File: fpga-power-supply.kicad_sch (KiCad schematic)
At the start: 30 parts, among them U14 XC7A100T-FGG484

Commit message: [#55652] Fix hotareas
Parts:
- C145, C151: Manufacturer Samsung -> Samsung Electro-Mechanics
- C150: value C_330u_KEMET_D -> C_Pol_330u_6.3V_KEMET-T520-D; footprint antmicro-footprints:KEMET_D -> antmicro-footprints:C_Pol_EIA-D; symbol antmicroCapacitorspol:C_330u_KEMET_D -> antmicroCapacitorspol:C_Pol_330u_6.3V_KEMET-T520-D; Voltage (none) -> 6.3V
- U14: footprint antmicro-footprints:BGA-484_23x23mm_Layout22x22_P1mm_Xilinx_FGG484 -> antmicro-footprints:BGA-484_23x23mm_Layout22x22_P1mm_FGG484; symbol antmicroMicrocontrollers:XC7A100T-FGG484 -> antmicroFPGAChips:XC7A100T-FGG484; Manufacturer Xilinx -> AMD-Xilinx

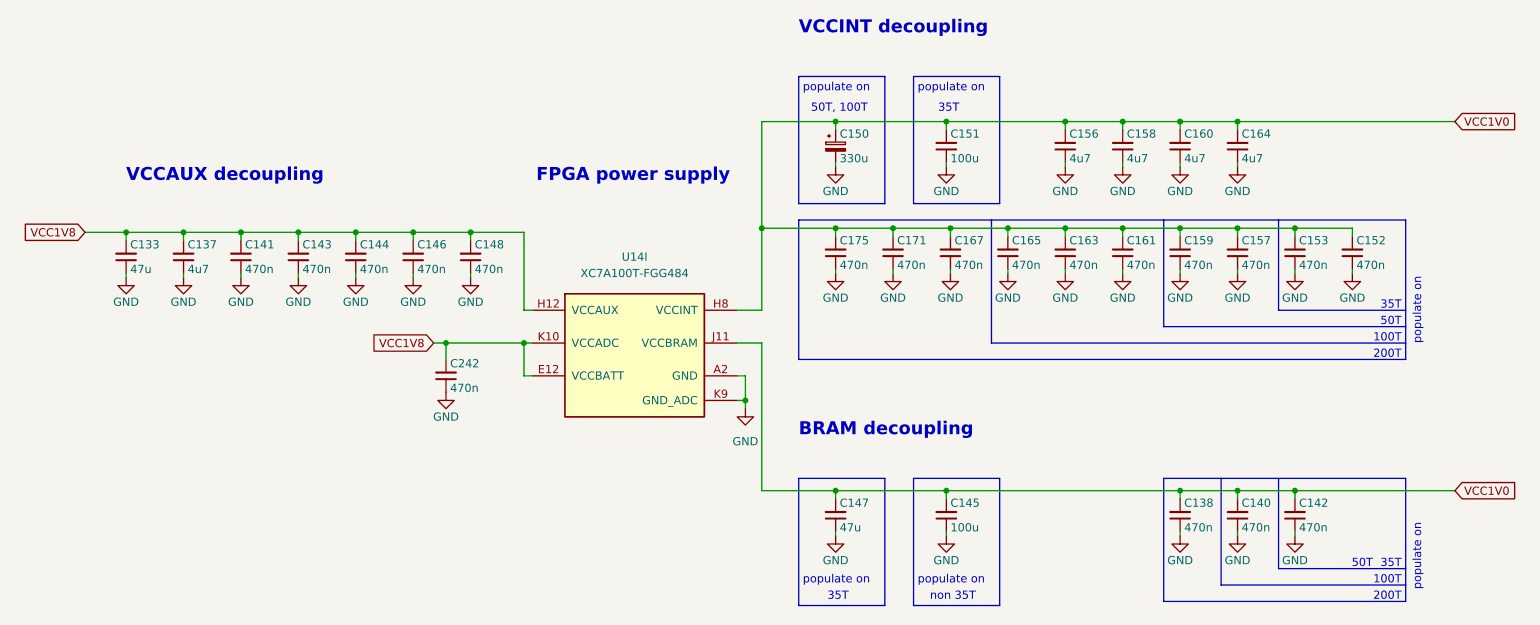
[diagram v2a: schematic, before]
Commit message: [#68236] Allign sch to grid
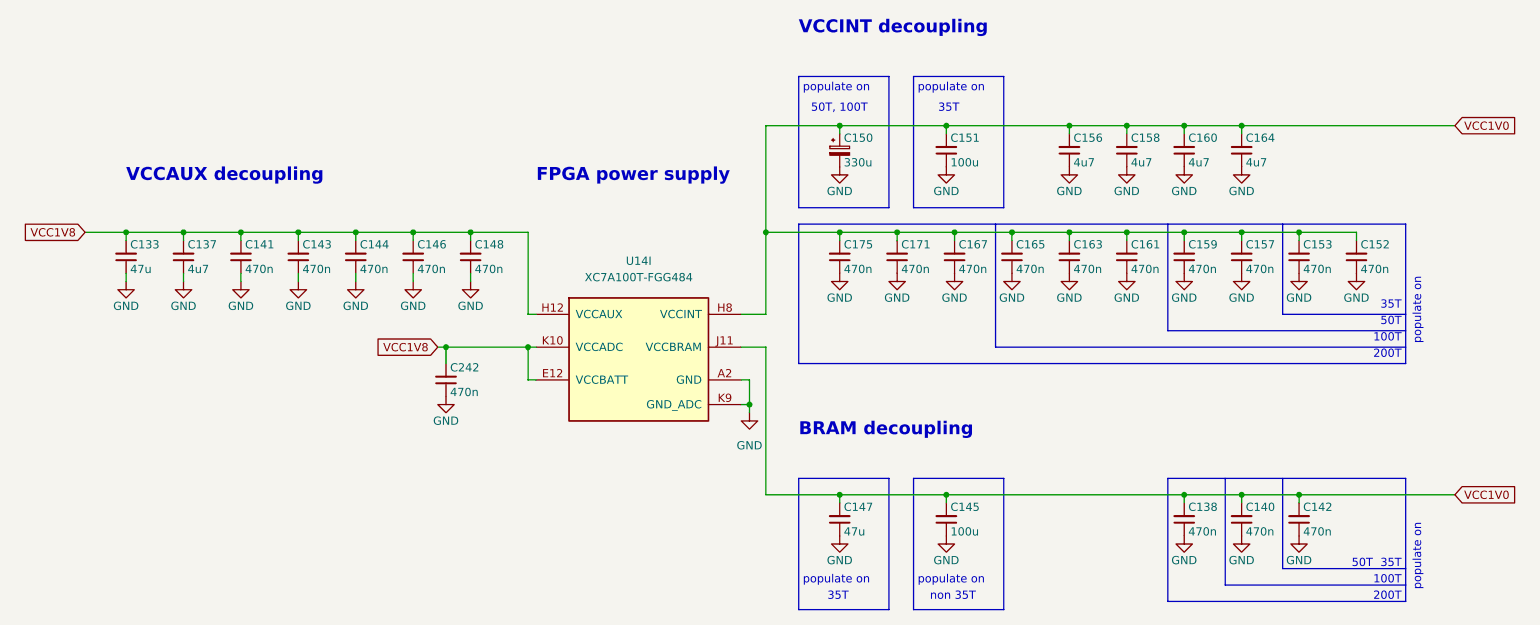
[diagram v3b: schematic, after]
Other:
- moved on the sheet: C138, C140, C142, C145, C147, C150, C151, C152, C153, C156, C157, C158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

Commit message: [#68236] Remove DNP property from Testpoints
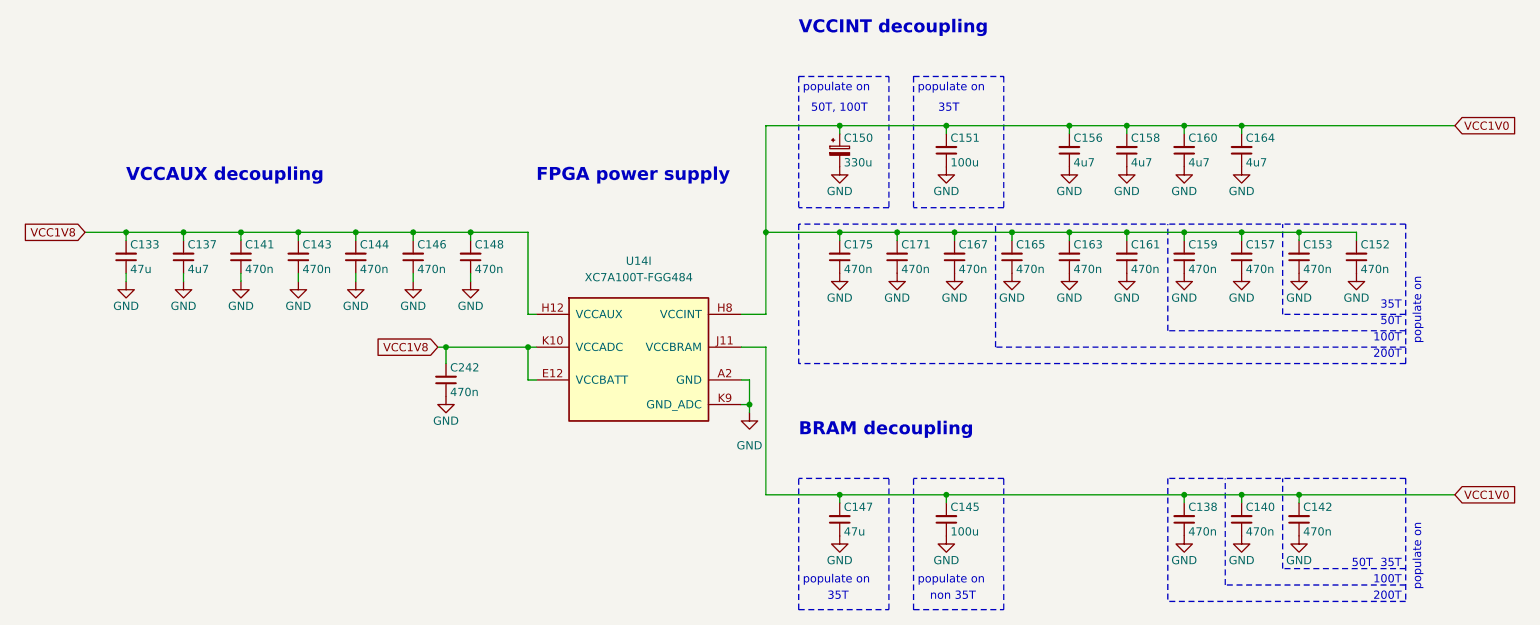
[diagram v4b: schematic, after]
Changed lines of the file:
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@@
   )
   (polyline (pts (xy 242.57 142.24) (xy 242.57 123.19))
-    (stroke (width 0) (type default))
+    (stroke (width 0) (type dash))
   )
   (polyline (pts (xy 306.07 179.07) (xy 278.13 179.07))
-    (stroke (width 0) (type default))
+    (stroke (width 0) (type dash))
   )
   (wire (pts (xy 161.29 124.46) (xy 161.29 125.73))
@@
   )
   (polyline (pts (xy 226.06 100.33) (xy 226.06 120.65))
-    (stroke (width 0) (type default))
+    (stroke (width 0) (type dash))
   )
   (wire (pts (xy 254 107.95) (xy 262.89 107.95))
@@
   )
   (polyline (pts (xy 287.02 137.16) (xy 287.02 123.19))
-    (stroke (width 0) (type default))
+    (stroke (width 0) (type dash))
   )
   (polyline (pts (xy 306.07 144.78) (xy 212.09 144.78))
-    (stroke (width 0) (type default))
+    (stroke (width 0) (type dash))
   )
   (polyline (pts (xy 306.07 142.24) (xy 242.57 142.24))
-    (stroke (width 0) (type default))
+    (stroke (width 0) (type dash))
   )
   (polyline (pts (xy 243.84 162.56) (xy 229.87 162.56))
-    (stroke (width 0) (type default))
+    (stroke (width 0) (type dash))
   )
   (polyline (pts (xy 306.07 144.78) (xy 306.07 123.19))
-    (stroke (width 0) (type default))
+    (stroke (width 0) (type dash))
   )
   (wire (pts (xy 156.21 142.24) (xy 157.48 142.24))
@@
   )
   (polyline (pts (xy 229.87 100.33) (xy 243.84 100.33))
-    (stroke (width 0) (type default))
+    (stroke (width 0) (type dash))
   )
   (wire (pts (xy 236.22 124.46) (xy 227.33 124.46))
@@
   )
   (polyline (pts (xy 287.02 176.53) (xy 287.02 162.56))
-    (stroke (width 0) (type default))
+    (stroke (width 0) (type dash))
   )
   (polyline (pts (xy 229.87 182.88) (xy 229.87 162.56))
-    (stroke (width 0) (type default))
+    (stroke (width 0) (type dash))
   )
   (wire (pts (xy 203.2 147.32) (xy 204.47 147.32))
@@
   )
   (polyline (pts (xy 306.07 162.56) (xy 306.07 181.61))
-    (stroke (width 0) (type default))
+    (stroke (width 0) (type dash))
   )
   (wire (pts (xy 280.67 124.46) (xy 271.78 124.46))
@@
   )
   (polyline (pts (xy 306.07 123.19) (xy 212.09 123.19))
-    (stroke (width 0) (type default))
+    (stroke (width 0) (type dash))
   )
   (polyline (pts (xy 226.06 120.65) (xy 212.09 120.65))
-    (stroke (width 0) (type default))
+    (stroke (width 0) (type dash))
   )
   (wire (pts (xy 203.2 137.16) (xy 207.01 137.16))
@@
   )
   (polyline (pts (xy 212.09 123.19) (xy 212.09 144.78))
-    (stroke (width 0) (type default))
+    (stroke (width 0) (type dash))
   )
   (wire (pts (xy 280.67 124.46) (xy 280.67 125.73))
@@
   )
   (polyline (pts (xy 212.09 182.88) (xy 226.06 182.88))
-    (stroke (width 0) (type default))
+    (stroke (width 0) (type dash))
   )
   (wire (pts (xy 289.56 124.46) (xy 280.67 124.46))
@@
   )
   (polyline (pts (xy 226.06 182.88) (xy 226.06 162.56))
-    (stroke (width 0) (type default))
+    (stroke (width 0) (type dash))
   )
   (wire (pts (xy 236.22 124.46) (xy 245.11 124.46))
@@
   )
   (polyline (pts (xy 229.87 182.88) (xy 243.84 182.88))
-    (stroke (width 0) (type default))
+    (stroke (width 0) (type dash))
   )
   (wire (pts (xy 170.18 147.32) (xy 171.45 147.32))
@@
   )
   (polyline (pts (xy 278.13 179.07) (xy 278.13 162.56))
-    (stroke (width 0) (type default))
+    (stroke (width 0) (type dash))
   )
   (wire (pts (xy 245.11 124.46) (xy 254 124.46))
@@
   )
   (polyline (pts (xy 306.07 176.53) (xy 287.02 176.53))
-    (stroke (width 0) (type default))
+    (stroke (width 0) (type dash))
   )
   (wire (pts (xy 157.48 142.24) (xy 157.48 144.78))
@@
   )
   (polyline (pts (xy 212.09 182.88) (xy 212.09 162.56))
-    (stroke (width 0) (type default))
+    (stroke (width 0) (type dash))
   )
   (wire (pts (xy 289.56 165.1) (xy 313.69 165.1))
@@
   )
   (polyline (pts (xy 306.07 162.56) (xy 269.24 162.56))
-    (stroke (width 0) (type default))
+    (stroke (width 0) (type dash))
   )
   (wire (pts (xy 280.67 165.1) (xy 280.67 166.37))
@@
   )
   (polyline (pts (xy 212.09 100.33) (xy 226.06 100.33))
-    (stroke (width 0) (type default))
+    (stroke (width 0) (type dash))
   )
   (wire (pts (xy 207.01 142.24) (xy 207.01 165.1))
@@
   )
   (polyline (pts (xy 212.09 100.33) (xy 212.09 120.65))
-    (stroke (width 0) (type default))
+    (stroke (width 0) (type dash))
   )
   (wire (pts (xy 254 107.95) (xy 254 109.22))
@@
   )
   (polyline (pts (xy 306.07 139.7) (xy 269.24 139.7))
-    (stroke (width 0) (type default))
+    (stroke (width 0) (type dash))
   )
   (wire (pts (xy 262.89 124.46) (xy 262.89 125.73))
@@
   )
   (polyline (pts (xy 226.06 162.56) (xy 212.09 162.56))
-    (stroke (width 0) (type default))
+    (stroke (width 0) (type dash))
   )
   (wire (pts (xy 204.47 147.32) (xy 204.47 151.13))
@@
   )
   (polyline (pts (xy 243.84 120.65) (xy 229.87 120.65))
-    (stroke (width 0) (type default))
+    (stroke (width 0) (type dash))
   )
   (wire (pts (xy 271.78 107.95) (xy 271.78 109.22))
@@
   )
   (polyline (pts (xy 269.24 162.56) (xy 269.24 181.61))
-    (stroke (width 0) (type default))
+    (stroke (width 0) (type dash))
   )
   (wire (pts (xy 125.73 124.46) (xy 125.73 125.73))
@@
   )
   (polyline (pts (xy 243.84 100.33) (xy 243.84 120.65))
-    (stroke (width 0) (type default))
+    (stroke (width 0) (type dash))
   )
   (wire (pts (xy 203.2 142.24) (xy 207.01 142.24))
@@
   )
   (polyline (pts (xy 243.84 182.88) (xy 243.84 162.56))
-    (stroke (width 0) (type default))
+    (stroke (width 0) (type dash))
   )
   (wire (pts (xy 125.73 124.46) (xy 134.62 124.46))
@@
   )
   (polyline (pts (xy 306.07 137.16) (xy 287.02 137.16))
-    (stroke (width 0) (type default))
+    (stroke (width 0) (type dash))
   )
   (wire (pts (xy 234.95 107.95) (xy 254 107.95))
@@
   )
   (polyline (pts (xy 229.87 100.33) (xy 229.87 120.65))
-    (stroke (width 0) (type default))
+    (stroke (width 0) (type dash))
   )
   (wire (pts (xy 143.51 130.81) (xy 143.51 132.08))
@@
   )
   (polyline (pts (xy 269.24 139.7) (xy 269.24 123.19))
-    (stroke (width 0) (type default))
+    (stroke (width 0) (type dash))
   )
   (polyline (pts (xy 306.07 181.61) (xy 269.24 181.61))
-    (stroke (width 0) (type default))
+    (stroke (width 0) (type dash))
   )
   (wire (pts (xy 271.78 107.95) (xy 280.67 107.95))
